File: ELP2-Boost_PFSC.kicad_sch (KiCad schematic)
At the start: 18 parts, among them J1 Screw_Terminal_01x03, J2 Screw_Terminal_01x03, Q1 12n50C3

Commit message: Changes:  - Added netclasses  - Better footprint for testpoints  - EMI filter
TODO:
 - Route the rest of the board
 - Different versions of the board to make sure its approved on monday
 - Get shunt footprint
 - Figure out wich connections can be jumpered
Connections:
- net Prot-EMI/N: now also J1.1 (Pin_1); no longer J1.3 (Pin_3)
- net Prot-EMI/P: now also J1.3 (Pin_3); no longer J1.1 (Pin_1)
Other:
- moved on the sheet: J1

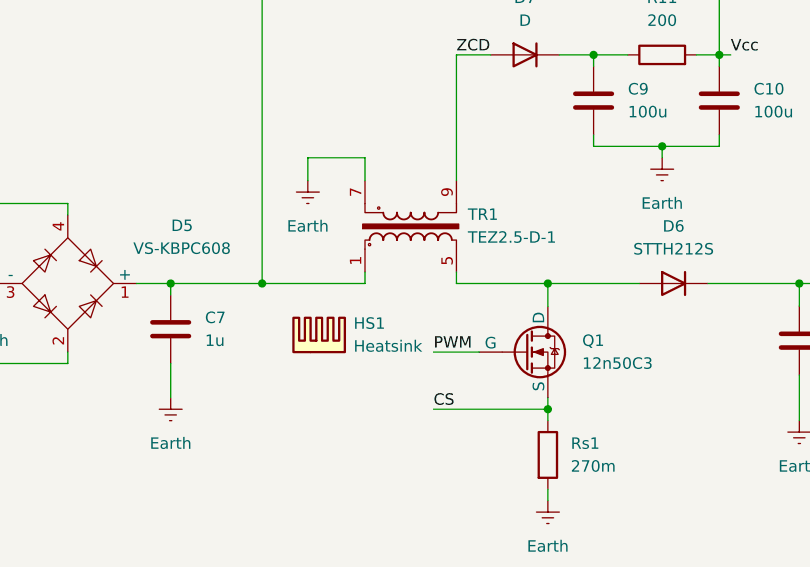
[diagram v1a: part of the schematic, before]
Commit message: Changed:  - Added basic routing/positioning  - Better netclasses  - Determined location for the IC TODO:  - Finish routing  - Add jumpers for voltage signals
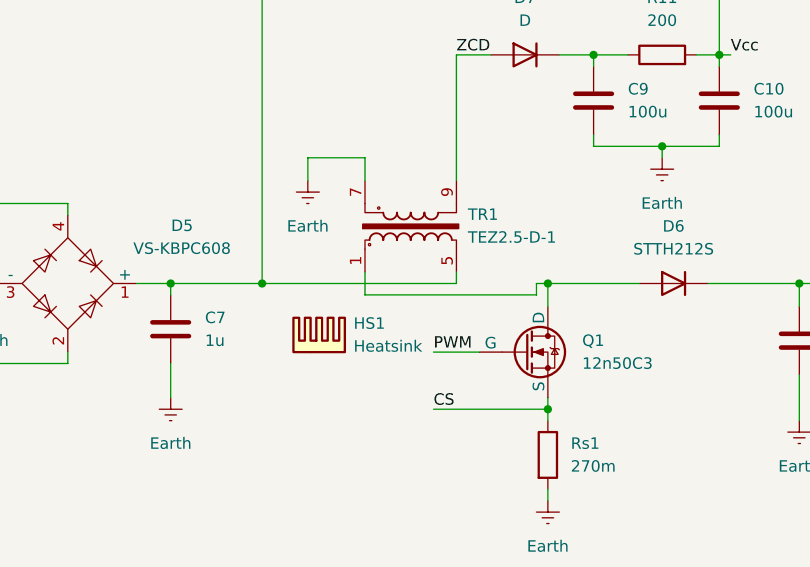
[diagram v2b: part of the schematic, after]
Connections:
- net at C7.1, D5.1 (+), R12.1: now also TR1.5; no longer TR1.1
- net at D6.2 (A), Q1.2 (D): now also TR1.1; no longer TR1.5
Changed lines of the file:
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@@
+	)
+	(junction
+		(at 102.87 69.85)
+		(diameter 0)
+		(color 0 0 0 0)
+	)
+	(junction
+		(at 91.44 77.47)
+		(diameter 0)
+		(color 0 0 0 0)
+	)
+	(junction
+		(at 180.34 43.18)
+		(diameter 0)
+		(color 0 0 0 0)
+	)
+	(junction
+		(at 187.96 53.34)
+		(diameter 0)
+		(color 0 0 0 0)
+	)
+	(junction
+		(at 203.2 68.58)
+		(diameter 0)
+		(color 0 0 0 0)
 	)
 	(junction
@@
 	)
 	(junction
-		(at 102.87 69.85)
-		(diameter 0)
-		(color 0 0 0 0)
-	)
-	(junction
-		(at 91.44 77.47)
-		(diameter 0)
-		(color 0 0 0 0)
-	)
-	(junction
-		(at 180.34 43.18)
-		(diameter 0)
-		(color 0 0 0 0)
-	)
-	(junction
 		(at 143.51 68.58)
 		(diameter 0)
 		(color 0 0 0 0)
 	)
-	(junction
-		(at 187.96 53.34)
-		(diameter 0)
-		(color 0 0 0 0)
-	)
-	(junction
-		(at 203.2 68.58)
-		(diameter 0)
-		(color 0 0 0 0)
-	)
 	(no_connect
 		(at 41.91 85.09)
@@
 	(wire
 		(pts
-			(xy 143.51 68.58) (xy 154.94 68.58)
-		)
-		(stroke
-			(width 0)
-			(type default)
-		)
-	)
-	(wire
-		(pts
 			(xy 175.26 68.58) (xy 185.42 68.58)
 		)
@@
 	(wire
 		(pts
+			(xy 173.99 68.58) (xy 175.26 68.58)
+		)
+		(stroke
+			(width 0)
+			(type default)
+		)
+	)
+	(wire
+		(pts
 			(xy 154.94 54.61) (xy 148.59 54.61)
 		)
@@
 	(wire
 		(pts
+			(xy 143.51 68.58) (xy 165.1 68.58)
+		)
+		(stroke
+			(width 0)
+			(type default)
+		)
+	)
+	(wire
+		(pts
 			(xy 203.2 68.58) (xy 203.2 71.12)
 		)
@@
 	(wire
 		(pts
+			(xy 165.1 67.31) (xy 165.1 68.58)
+		)
+		(stroke
+			(width 0)
+			(type default)
+		)
+	)
+	(wire
+		(pts
 			(xy 133.35 68.58) (xy 143.51 68.58)
 		)
@@
 	(wire
 		(pts
-			(xy 154.94 67.31) (xy 154.94 68.58)
-		)
-		(stroke
-			(width 0)
-			(type default)
-		)
-	)
-	(wire
-		(pts
 			(xy 203.2 68.58) (xy 224.79 68.58)
 		)
@@
 	(wire
 		(pts
-			(xy 165.1 67.31) (xy 165.1 68.58)
-		)
-		(stroke
-			(width 0)
-			(type default)
-		)
-	)
-	(wire
-		(pts
 			(xy 176.53 43.18) (xy 180.34 43.18)
 		)
@@
 	(wire
 		(pts
+			(xy 154.94 67.31) (xy 154.94 69.85)
+		)
+		(stroke
+			(width 0)
+			(type default)
+		)
+	)
+	(wire
+		(pts
 			(xy 35.56 71.12) (xy 39.37 71.12)
 		)
@@
 	(wire
 		(pts
+			(xy 154.94 69.85) (xy 173.99 69.85)
+		)
+		(stroke
+			(width 0)
+			(type default)
+		)
+	)
+	(wire
+		(pts
+			(xy 173.99 69.85) (xy 173.99 68.58)
+		)
+		(stroke
+			(width 0)
+			(type default)
+		)
+	)
+	(wire
+		(pts
 			(xy 180.34 53.34) (xy 187.96 53.34)
 		)
@@
 		(pts
 			(xy 91.44 88.9) (xy 96.52 88.9)
-		)
-		(stroke
-			(width 0)
-			(type default)
-		)
-	)
-	(wire
-		(pts
-			(xy 165.1 68.58) (xy 175.26 68.58)
 		)
 		(stroke
@@
 			(justify left bottom)
 		)
-		(property "Netclass" "HV_HC"
+		(property "Netclass" "HV_LC"
 			(at 145.4785 66.04 0)
 			(effects

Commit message: Placa refeita de acordo com pedidos do professor, sujeita a alteração
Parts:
- C7: footprint Capacitor_THT:C_Rect_L7.2mm_W3.5mm_P5.00mm_FKS2_FKP2_MKS2_MKP2 -> Capacitor_THT:C_Rect_L31.5mm_W9.0mm_P27.50mm_MKS4
- R11, R12, R13: footprint Resistor_THT:R_Axial_DIN0207_L6.3mm_D2.5mm_P15.24mm_Horizontal -> Resistor_THT:R_Axial_DIN0207_L6.3mm_D2.5mm_P10.16mm_Horizontal
- Rs1: footprint (none) -> Resistor_SMD:R_2512_6332Metric_Pad1.40x3.35mm_HandSolder
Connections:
- net Earth: now also TR1.5; no longer TR1.7
- net ZCD: now also TR1.1; no longer TR1.9
- net at D6.2 (A), Q1.2 (D): now also TR1.7; no longer TR1.1
- net at C7.1, D5.1 (+), R12.1: now also TR1.9; no longer TR1.5
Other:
- moved on the sheet: TR1

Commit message: Ajustes nos planos de referência e posição do shunt
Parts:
- C8: footprint Capacitor_THT:C_Radial_D10.0mm_H20.0mm_P5.00mm -> Capacitor_THT:CP_Radial_D22.0mm_P10.00mm_SnapIn
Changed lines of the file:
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@@
 			)
 		)
-		(property "Footprint" "Capacitor_THT:C_Radial_D10.0mm_H20.0mm_P5.00mm"
+		(property "Footprint" "Capacitor_THT:CP_Radial_D22.0mm_P10.00mm_SnapIn"
 			(at 204.1652 78.74 0)
 			(effects

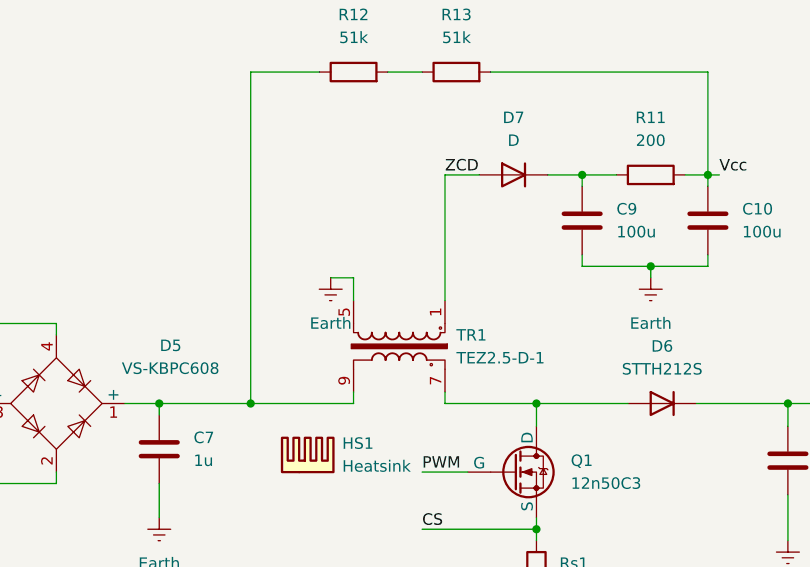
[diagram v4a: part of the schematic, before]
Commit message: Got all the blocks a lot closer and named the testpoints on the silkscreen
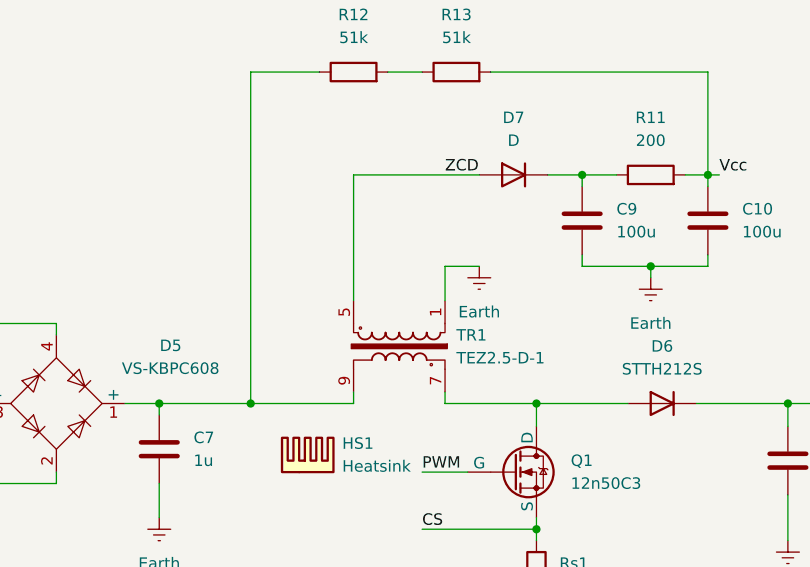
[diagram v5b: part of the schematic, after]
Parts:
- TR1: symbol Transformer:TEZ2.5-D-1 -> ELP-Boost_PFC:Indutor-Transformador
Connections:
- net Earth: now also TR1.1; no longer TR1.5
- net ZCD: now also TR1.5; no longer TR1.1
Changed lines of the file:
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@@
+	(wire
+		(pts
+			(xy 165.1 53.34) (xy 165.1 57.15)
+		)
+		(stroke
+			(width 0)
+			(type default)
+		)
+	)
 	(wire
 		(pts
@@
 	(wire
 		(pts
-			(xy 165.1 43.18) (xy 168.91 43.18)
-		)
-		(stroke
-			(width 0)
-			(type default)
-		)
-	)
-	(wire
-		(pts
 			(xy 39.37 77.47) (xy 41.91 77.47)
 		)
@@
 	(wire
 		(pts
-			(xy 165.1 43.18) (xy 165.1 57.15)
-		)
-		(stroke
-			(width 0)
-			(type default)
-		)
-	)
-	(wire
-		(pts
 			(xy 182.88 140.97) (xy 182.88 142.24)
 		)
@@
 	(wire
 		(pts
+			(xy 165.1 53.34) (xy 168.91 53.34)
+		)
+		(stroke
+			(width 0)
+			(type default)
+		)
+	)
+	(wire
+		(pts
 			(xy 35.56 71.12) (xy 39.37 71.12)
 		)
@@
 	(wire
 		(pts
+			(xy 154.94 57.15) (xy 154.94 43.18)
+		)
+		(stroke
+			(width 0)
+			(type default)
+		)
+	)
+	(wire
+		(pts
 			(xy 191.77 43.18) (xy 194.31 43.18)
 		)
@@
 	(wire
 		(pts
-			(xy 154.94 54.61) (xy 154.94 57.15)
+			(xy 154.94 43.18) (xy 168.91 43.18)
 		)
 		(stroke
@@
 		(pts
 			(xy 96.52 88.9) (xy 102.87 88.9)
-		)
-		(stroke
-			(width 0)
-			(type default)
-		)
-	)
-	(wire
-		(pts
-			(xy 154.94 54.61) (xy 152.4 54.61)
 		)
 		(stroke
@@
 		(length 2.54)
 		(shape round)
+		(at 160.02 31.75 180)
+		(fields_autoplaced yes)
+		(effects
+			(font
+				(size 1.27 1.27)
+			)
+			(justify right bottom)
+		)
+		(property "Netclass" "HV_LC"
+			(at 160.7185 34.29 0)
+			(effects
+				(font
+					(size 1.27 1.27)
+				)
+				(justify left)
+			)
+		)
+		(property "Component Class" ""
+			(at 13.97 125.73 0)
+			(effects
+				(font
+					(size 1.27 1.27)
+					(italic yes)
+				)
+			)
+		)
+	)
+	(netclass_flag ""
+		(length 2.54)
+		(shape round)
 		(at 39.37 69.85 0)
 		(fields_autoplaced yes)
@@
 	)
 	(symbol
-		(lib_id "Transformer:TEZ2.5-D-1")
-		(at 160.02 62.23 270)
+		(lib_id "ELP-Boost_PFC:Indutor-Transformador")
+		(at 167.64 57.15 270)
 		(unit 1)
 		(exclude_from_sim no)
@@
 		)
 		(property "Footprint" "ELP-Boost_PFC:Indutor ELP"
-			(at 151.13 62.23 0)
-			(effects
-				(font
-					(size 1.27 1.27)
-					(italic yes)
+			(at 167.64 57.15 0)
+			(effects
+				(font
+					(size 1.27 1.27)
 				)
 				(hide yes)
@@
 		)
 		(property "Datasheet" "http://www.breve.pl/pdf/ANG/TEZ_ang.pdf"
-			(at 160.02 62.23 0)
+			(at 167.64 57.15 0)
 			(effects
 				(font
@@
 		)
 		(property "Description" "TEZ2.5/D/x, 2.5VA, Single Secondary, Cast Resin Transformer, PCB"
-			(at 160.02 62.23 0)
+			(at 167.64 57.15 0)
 			(effects
 				(font
@@
 	(symbol
 		(lib_id "power:Earth")
-		(at 152.4 54.61 0)
+		(at 168.91 53.34 0)
+		(mirror y)
 		(unit 1)
 		(exclude_from_sim no)
@@
 		(fields_autoplaced yes)
 		(property "Reference" "#PWR013"
-			(at 152.4 60.96 0)
+			(at 168.91 59.69 0)
 			(effects
 				(font
@@
 		)
 		(property "Value" "Earth"
-			(at 152.4 59.69 0)
+			(at 168.91 58.42 0)
 			(effects
 				(font
@@
 		)
 		(property "Footprint" ""
-			(at 152.4 54.61 0)
+			(at 168.91 53.34 0)
 			(effects
 				(font
@@
 		)
 		(property "Datasheet" "~"
-			(at 152.4 54.61 0)
+			(at 168.91 53.34 0)
 			(effects
 				(font
@@
 		)
 		(property "Description" "Power symbol creates a global label with name \"Earth\""
-			(at 152.4 54.61 0)
-			(effects
-				(font
+			(at 168.91 53.34 0)
+			(effects
+				(font
